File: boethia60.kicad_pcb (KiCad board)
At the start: 2 copper layers, 286.7 x 102.7 mm, 154 parts, among them J1 Conn_01x06, SW1 SW_Push, SW10 #8, SW11 #9, SW12 #0, SW13 -_, SW14 =+, SW15 \|, SW16 `~, SW17 Tab, SW18 Q, SW19 W, SW2 Esc, SW20 E, SW21 R, SW22 T, SW23 Y, SW24 U, SW25 I, SW26 O, SW27 P, SW28 [{, SW29 ]}, SW3 #1, SW30 Bksp, SW31 Ctrl, SW32 A, SW33 S, SW34 D, SW35 F, SW36 G, SW37 H, SW38 J, SW39 K, SW4 #2, SW40 L, SW41 ;:, SW42 '", SW43 Enter, SW44 Shift, SW45 Z, SW46 X, SW47 C, SW48 V, SW49 B, SW5 #3, SW50 N, SW51 M, SW52 ,<, SW53 .>, SW54 /?, SW55 Shift, SW56 Fn, SW57 Win, SW58 Alt, SW59 Space, SW6 #4, SW60 Alt, SW61 Ctrl, SW7 #5, SW8 #6, SW9 #7, U1 NCP1117-3.3_SOT223, U2 PRTR5V0U2X, U3 RP2040, U4 W25Q128JVS, Y1 Crystal_GND24_Small

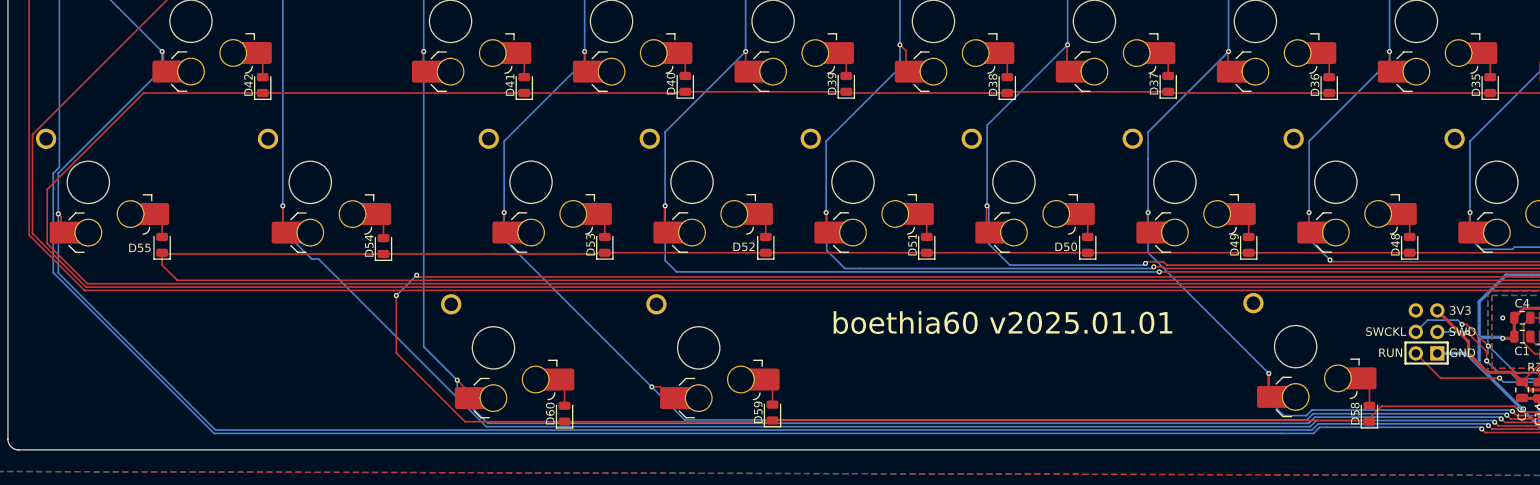
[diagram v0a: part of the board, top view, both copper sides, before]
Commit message: Fixed lonely column.
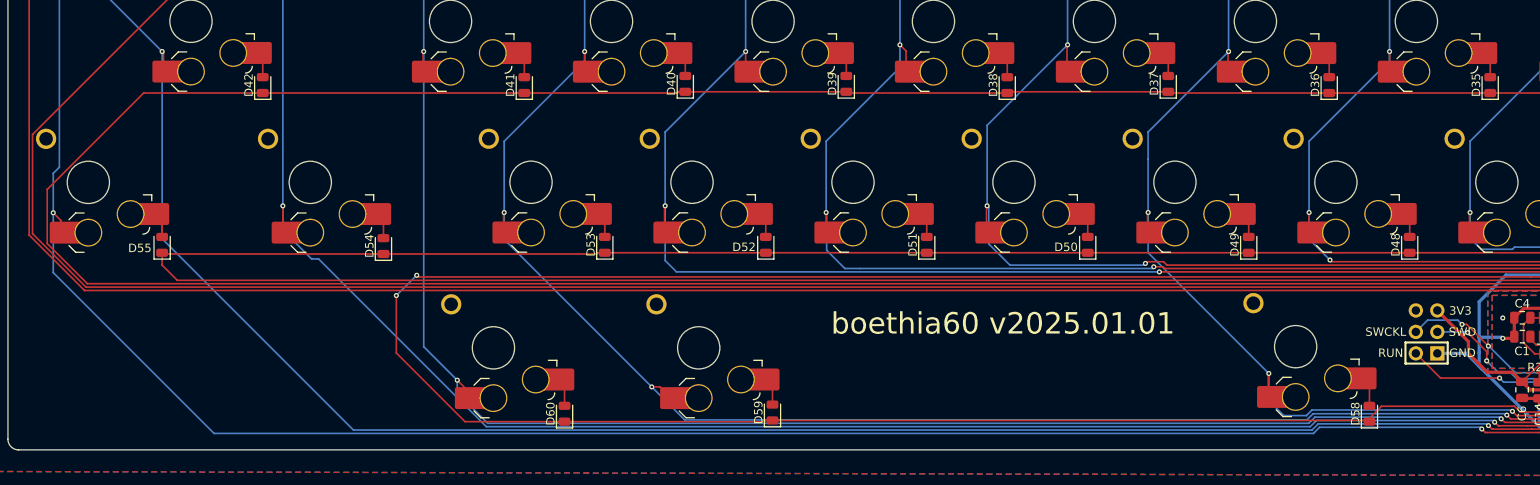
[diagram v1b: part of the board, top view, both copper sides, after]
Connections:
- SW56 pad 2: col13 -> col14
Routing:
- net col13: track 279.6 -> 257.5 mm, vias 5 -> 4
- net col14: track 259.3 -> 262.0 mm, vias 2 -> 3
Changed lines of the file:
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@@
 			(layers "F.Cu" "F.Paste" "F.Mask")
 			(roundrect_rratio 0.1)
-			(net 93 "col13")
+			(net 94 "col14")
 			(pinfunction "2")
 			(pintype "passive")
@@
 			(size 1.2 2.6)
 			(layers "F.Cu")
-			(net 93 "col13")
+			(net 94 "col14")
 			(pinfunction "2")
 			(pintype "passive")
@@
 			(layers "*.Cu" "F.Mask")
 			(remove_unused_layers no)
-			(net 93 "col13")
+			(net 94 "col14")
 			(pinfunction "2")
 			(pintype "passive")
@@
 	)
 	(segment
-		(start 3.105 85.401)
-		(end 3.105 87.3125)
-		(width 0.2)
-		(layer "F.Cu")
-		(net 93)
-	)
-	(segment
-		(start 2.794 85.09)
-		(end 3.105 85.401)
-		(width 0.2)
-		(layer "F.Cu")
-		(net 93)
-	)
-	(segment
 		(start 22.155 30.0925)
 		(end 22.225 30.1625)
@@
 	)
 	(via
-		(at 2.794 85.09)
-		(size 0.6)
-		(drill 0.3)
-		(layers "F.Cu" "B.Cu")
-		(net 93)
-	)
-	(via
 		(at 19.84375 31.94375)
 		(size 0.6)
@@
 	)
 	(segment
-		(start 151.892 109.945524)
-		(end 151.163524 110.674)
-		(width 0.2)
-		(layer "B.Cu")
-		(net 93)
-	)
-	(segment
 		(start 18.388241 31.94375)
 		(end 7.9375 42.394491)
@@
 	)
 	(segment
-		(start 15.08125 67.97675)
-		(end 4.191 78.867)
-		(width 0.2)
-		(layer "B.Cu")
-		(net 93)
-	)
-	(segment
-		(start 21.393 110.674)
-		(end 2.794 92.075)
+		(start 37.719 110.674)
+		(end 151.163524 110.674)
 		(width 0.2)
 		(layer "B.Cu")
@@
 	)
 	(segment
-		(start 4.191 78.867)
-		(end 2.794 80.264)
+		(start 171.840542 109.945524)
+		(end 172.040542 110.145524)
 		(width 0.2)
 		(layer "B.Cu")
@@
 	)
 	(segment
-		(start 2.794 80.264)
-		(end 2.794 85.09)
-		(width 0.2)
-		(layer "B.Cu")
-		(net 93)
-	)
-	(segment
-		(start 15.08125 65.88125)
-		(end 15.08125 67.97675)
-		(width 0.2)
-		(layer "B.Cu")
-		(net 93)
-	)
-	(segment
 		(start 7.9375 42.394491)
 		(end 7.9375 46.83125)
@@
 	)
 	(segment
-		(start 172.040542 110.145524)
+		(start 151.892 109.945524)
 		(end 171.840542 109.945524)
 		(width 0.2)
@@
 	)
 	(segment
-		(start 171.840542 109.945524)
-		(end 151.892 109.945524)
+		(start 15.08125 88.03625)
+		(end 37.719 110.674)
 		(width 0.2)
 		(layer "B.Cu")
@@
 	)
 	(segment
-		(start 2.794 92.075)
-		(end 2.794 85.09)
+		(start 151.163524 110.674)
+		(end 151.892 109.945524)
 		(width 0.2)
 		(layer "B.Cu")
@@
 	)
 	(segment
-		(start 151.163524 110.674)
-		(end 21.393 110.674)
+		(start 15.08125 65.88125)
+		(end 15.08125 88.03625)
 		(width 0.2)
 		(layer "B.Cu")
@@
 	)
 	(segment
+		(start 2.194 84.963)
+		(end 3.105 85.874)
+		(width 0.2)
+		(layer "F.Cu")
+		(net 94)
+	)
+	(segment
 		(start 171.670242 110.966)
 		(end 171.249766 110.545524)
@@
 	)
 	(segment
+		(start 3.105 85.874)
+		(end 3.105 87.3125)
+		(width 0.2)
+		(layer "F.Cu")
+		(net 94)
+	)
+	(segment
 		(start 185.039 107.061)
 		(end 181.134 110.966)
@@
 	)
 	(via
-		(at 2.921 32.639)
+		(at 2.194 84.963)
 		(size 0.6)
 		(drill 0.3)
@@
 		(net 94)
 	)
-	(segment
-		(start 2.921 79.571314)
-		(end 2.921 32.639)
-		(width 0.2)
-		(layer "B.Cu")
+	(via
+		(at 2.921 32.639)
+		(size 0.6)
+		(drill 0.3)
+		(layers "F.Cu" "B.Cu")
 		(net 94)
 	)
 	(segment
-		(start 171.249766 110.545524)
-		(end 171.049766 110.345524)
+		(start 152.057686 110.345524)
+		(end 151.32921 111.074)
 		(width 0.2)
 		(layer "B.Cu")
@@
 	)
 	(segment
-		(start 21.227314 111.074)
-		(end 2.194 92.040686)
+		(start 2.194 80.298314)
+		(end 2.921 79.571314)
 		(width 0.2)
 		(layer "B.Cu")
@@
 	(segment
 		(start 171.049766 110.345524)
-		(end 152.908 110.345524)
+		(end 152.057686 110.345524)
 		(width 0.2)
 		(layer "B.Cu")
@@
 	)
 	(segment
-		(start 151.839105 110.564105)
-		(end 151.32921 111.074)
+		(start 2.194 92.040686)
+		(end 2.194 80.298314)
 		(width 0.2)
 		(layer "B.Cu")
@@
 	)
 	(segment
-		(start 151.32921 111.074)
-		(end 147.574 111.074)
+		(start 171.249766 110.545524)
+		(end 171.049766 110.345524)
 		(width 0.2)
 		(layer "B.Cu")
@@
 	)
 	(segment
-		(start 147.574 111.074)
+		(start 151.32921 111.074)
 		(end 21.227314 111.074)
 		(width 0.2)
@@
 	)
 	(segment
-		(start 2.194 80.298314)
-		(end 2.921 79.571314)
-		(width 0.2)
-		(layer "B.Cu")
-		(net 94)
-	)
-	(segment
-		(start 152.908 110.345524)
-		(end 152.057686 110.345524)
-		(width 0.2)
-		(layer "B.Cu")
-		(net 94)
-	)
-	(segment
-		(start 152.057686 110.345524)
-		(end 151.839105 110.564105)
+		(start 21.227314 111.074)
+		(end 2.194 92.040686)
 		(width 0.2)
 		(layer "B.Cu")
@@
 	)
 	(segment
-		(start 2.194 92.040686)
-		(end 2.194 80.298314)
+		(start 2.921 79.571314)
+		(end 2.921 32.639)
 		(width 0.2)
 		(layer "B.Cu")

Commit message: Change footprints, fix errors, WIP BOM.
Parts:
- C1, C10, C11, C12, C13, C14, C15, C16, C4, C5, C6, C7, C8, C9: footprint Capacitor_SMD:C_0805_2012Metric -> Capacitor_SMD:C_0402_1005Metric
- C2, C3: value 10u -> 1u; footprint Capacitor_SMD:C_0805_2012Metric -> Capacitor_SMD:C_0402_1005Metric
- D1, D10, D11, D12, D13, D14, D15, D16, D17, D18, D19, D2, D20, D21, D22, D23, D24, D25, D26, D27, D28, D29, D3, D30, D31, D32, D33, D34, D35, D36, D37, D38, D39, D4, D40, D41, D42, D43, D44, D45, D46, D47, D48, D49, D5, D50, D51, D52, D53, D54, D55, D56, D57, D58, D59, D6, D60, D7, D8, D9: footprint Diode_SMD:D_0805_2012Metric -> Diode_SMD:D_SOD-323
- F1: footprint Fuse:Fuse_1206_3216Metric -> Fuse:Fuse_0805_2012Metric
- FB1: footprint Inductor_SMD:L_0805_2012Metric -> Inductor_SMD:L_0603_1608Metric
- R1, R2, R3, R4, R5, R6, R7: footprint Resistor_SMD:R_0805_2012Metric -> Resistor_SMD:R_0402_1005Metric
- SW13: value -_ -> Minus
- SW14: value =+ -> Equals
- SW15: value \| -> Backslash
- SW16: value `~ -> Grave
- SW41: value ;: -> Semi
- SW42: value '" -> Quote
- SW52: value ,< -> Comma
- SW53: value .> -> Dot
- SW54: value /? -> Slash
- moved C12 3.88 mm to (197.0, 107.5), turned to 0 degrees
- moved C10 2.21 mm to (197.1, 106.5)
- moved C3 2.07 mm to (279.5, 86.6)
- moved C6 2.03 mm to (178.1, 105.9)
- moved C15 1.91 mm to (197.1, 96.5)
- moved C2 1.40 mm to (277.5, 75.7)
- moved C4 1.25 mm to (177.3, 97.3), turned to -90 degrees
- moved C5 1.18 mm to (197.1, 105.5)
- moved C14 1.02 mm to (179.1, 105.9)
- moved C1 0.89 mm to (176.8, 100.1)
- moved C8 0.89 mm to (197.1, 97.5)
- moved R2 0.77 mm to (180.1, 101.2)
- moved C16 0.70 mm to (201.3, 99.2)
- moved R7 0.67 mm to (205.7, 104.7)
- moved C7 0.63 mm to (186.5, 107.5)
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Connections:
- U3 pad 2: GPIO0 -> col0
- U3 pad 27: col6 -> GPIO0
- U3 pad 3: GPIO1 -> col1
- U3 pad 34: col0 -> GPIO22
- U3 pad 35: col1 -> GPIO23
- U3 pad 36: col2 -> GPIO24
- U3 pad 4: GPIO2 -> col2
- U3 pad 5: GPIO3 -> col6
- U3 pad 6: GPIO4 -> GPIO1
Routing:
- net col6: track 147.7 -> 175.2 mm
- net col1: track 167.8 -> 148.4 mm
- net col11: track 232.1 -> 249.3 mm, vias 5 -> 7
- net GND: track 336.3 -> 319.2 mm, vias 14 -> 22
- net col10: track 221.0 -> 238.0 mm
- net col2: track 142.9 -> 126.8 mm
- net col0: track 159.5 -> 143.6 mm
- net /SD3: track 17.4 -> 12.6 mm
- net /SCLK: track 16.4 -> 12.6 mm
- net +3V3: track 226.2 -> 229.5 mm
- net /CS: track 38.1 -> 34.9 mm
- net /SD0: track 15.6 -> 12.9 mm
- net /SD2: track 26.6 -> 23.9 mm
- net /SD1: track 28.6 -> 26.0 mm
- net col13: track 257.5 -> 259.7 mm, vias 4 -> 6
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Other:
- board size 286.7 x 102.7 mm -> 286.7 x 100.6 mm
- board text added: "by arviceblot"

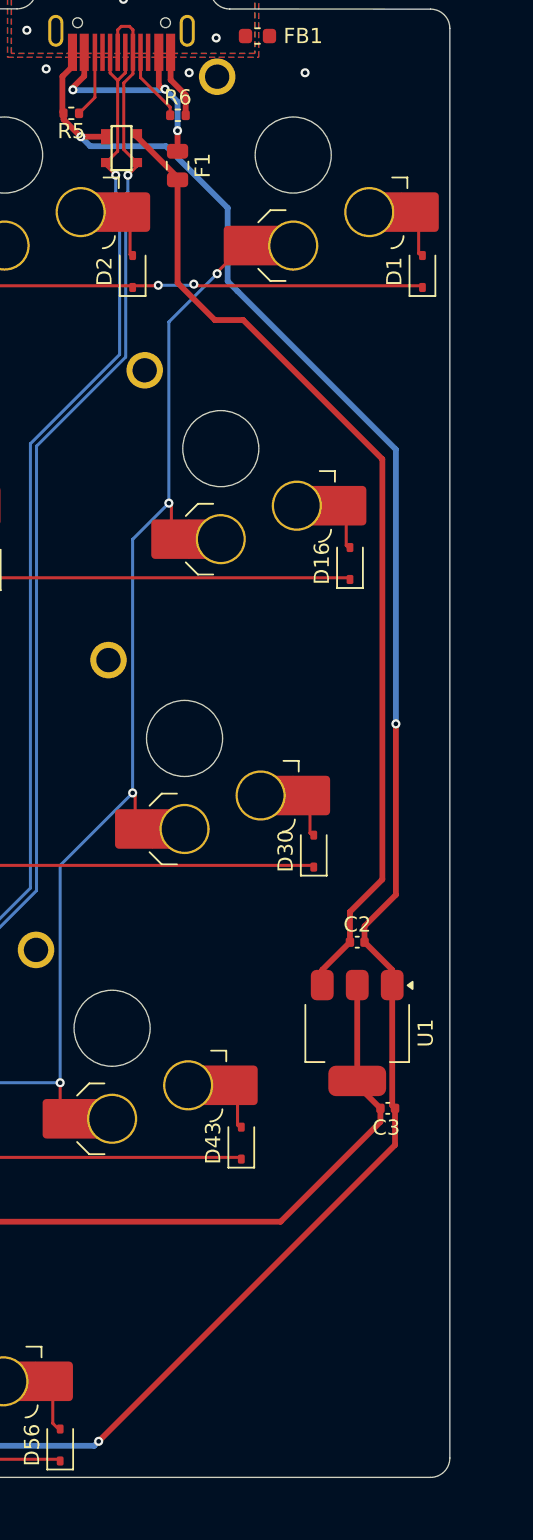
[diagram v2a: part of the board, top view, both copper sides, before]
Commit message: Fix firmware pins.
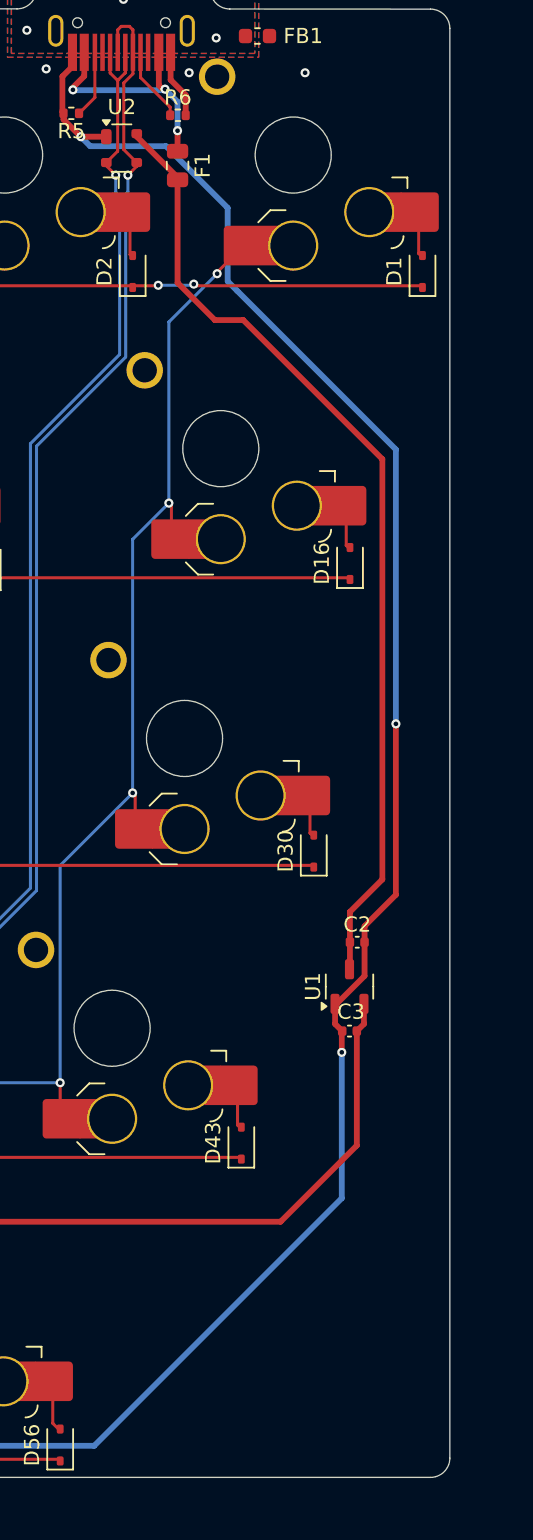
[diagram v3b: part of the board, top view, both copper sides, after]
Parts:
- U1: footprint Package_TO_SOT_SMD:SOT-223-3_TabPin2 -> Package_TO_SOT_SMD:SOT-23-3
- U2: footprint random-keyboard-parts:SOT143B -> Package_TO_SOT_SMD:SOT-143
- moved C3 5.67 mm to (277.0, 81.5), turned to 180 degrees
- moved U1 3.10 mm to (277.0, 78.6), turned to 90 degrees
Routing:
- net +3V3: track 229.5 -> 227.2 mm
- net +5V: track 65.5 -> 63.6 mm
- net GND: track 319.2 -> 318.0 mm
